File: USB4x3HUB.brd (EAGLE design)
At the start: 90 x 90 mm, 114 parts, among them IC1 TUSB2036, IC10 SN74LVC1G139DCUR, IC2 FSUSB74MPX, IC6 3.3V, IC7 5V, IC8 5V, IC9 5V, Q1 OSC4_6.0M, SW1 RD, SW2 BL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

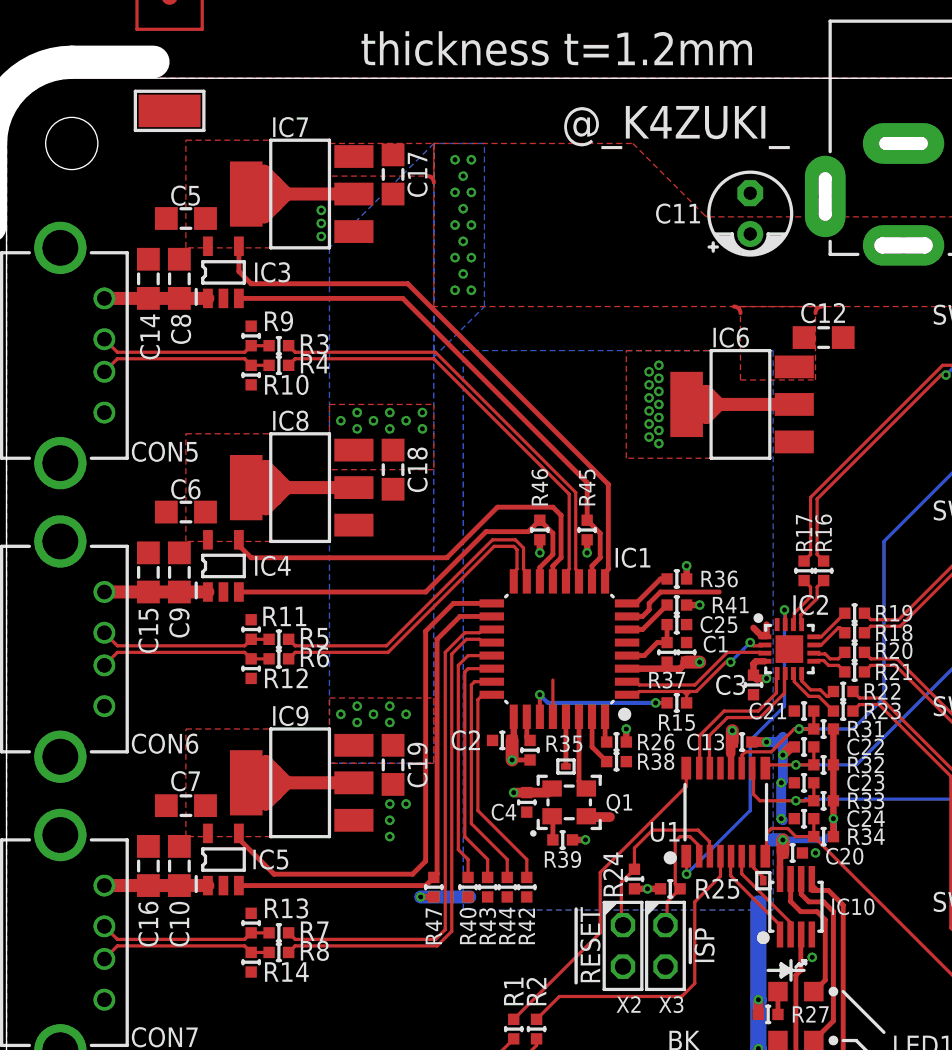
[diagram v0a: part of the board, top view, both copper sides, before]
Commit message: replace IC6-9 *CAUTION: airwires remain*
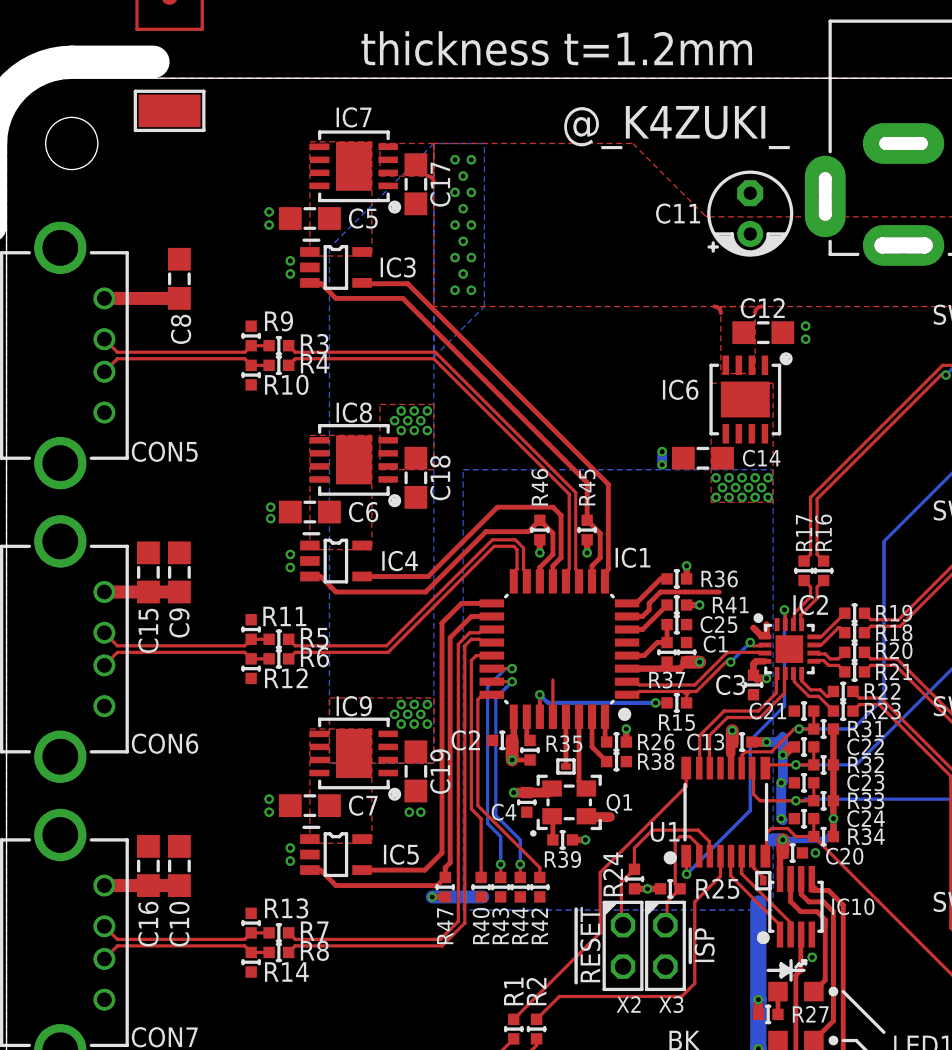
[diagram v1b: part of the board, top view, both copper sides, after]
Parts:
- IC6, IC7, IC8, IC9: device mylib:IC_SOT223 -> mylib:DFN80P410X410_8N
- moved C14 35.7 mm to (52.7, 56.7), turned to 180 degrees
- moved C5 7.60 mm to (28.6, 71.4)
- moved C6 7.60 mm to (28.6, 53.4)
- moved C7 7.60 mm to (28.6, 35.4)
- moved IC3 6.91 mm to (30.2, 68.4), turned to 270 degrees
- moved IC4 6.91 mm to (30.2, 50.4), turned to 270 degrees
- moved IC5 6.91 mm to (30.2, 32.4), turned to 270 degrees
- moved IC9 3.76 mm to (31.3, 38.6)
- moved C12 3.71 mm to (56.4, 64.4)
- moved IC8 3.71 mm to (31.3, 56.6)
- moved IC7 3.71 mm to (31.3, 74.6)
- moved C17 1.52 mm to (35.1, 73.5)
- moved C18 1.49 mm to (35.1, 55.5)
- moved C19 1.46 mm to (35.1, 37.5)
- moved R40 0.80 mm to (39.1, 30.4)
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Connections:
- net 3.3V: now also C14.1, IC6.5, IC6.6, IC6.7, IC6.EP; no longer IC6.2, IC6.4
- net 5V1: now also IC7.5, IC7.6, IC7.7, IC7.EP; no longer IC7.2, IC7.4
- net 5V2: now also IC8.5, IC8.6, IC8.7, IC8.EP; no longer IC8.2, IC8.4
- net 5V3: now also IC9.5, IC9.6, IC9.7, IC9.EP; no longer IC9.2, IC9.4
- net N$11: no longer C14.1
- net VIN: now also IC6.2, IC6.4, IC7.2, IC7.4, IC8.2, IC8.4, IC9.2, IC9.4
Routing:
- net 5V1: track 12.3 -> 0.00 mm
- net 5V3: track 11.8 -> 0.00 mm
- net 5V2: track 11.8 -> 0.00 mm
- net 3.3V: track 69.0 -> 58.6 mm, vias 32 -> 33
- net N$17: track 35.6 -> 26.2 mm
- net N$24: track 31.9 -> 23.0 mm
- net N$21: track 26.2 -> 18.4 mm
- net N$25: track 30.8 -> 26.8 mm
- net N$20: track 24.7 -> 20.7 mm
- net N$16: track 32.6 -> 28.7 mm
- net N$13: track 6.35 -> 4.60 mm
- net N$12: track 6.35 -> 4.60 mm
- net N$11: track 6.35 -> 4.60 mm
- net GND: track 21.1 -> 21.9 mm, vias 17 -> 28
- net N$64: track 15.5 -> 14.9 mm
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
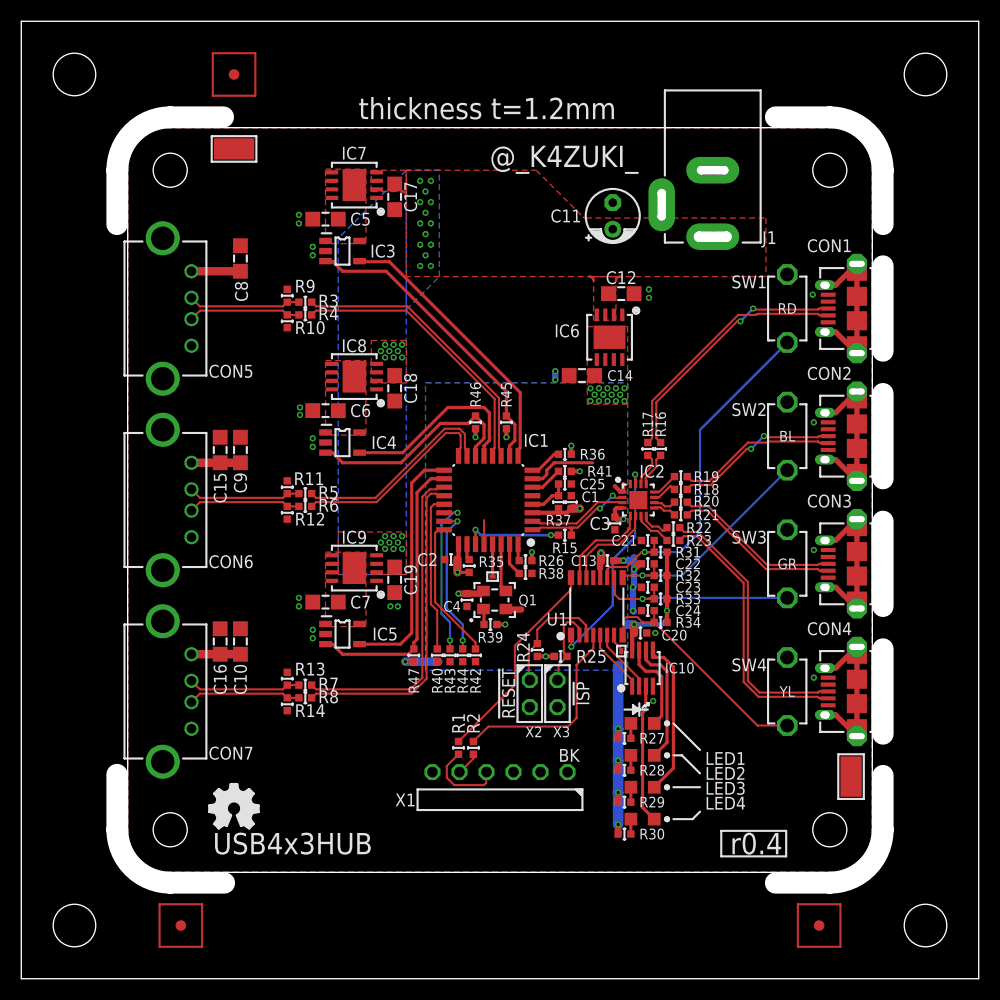
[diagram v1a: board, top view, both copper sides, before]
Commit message: C11: library update, C5-7 moved
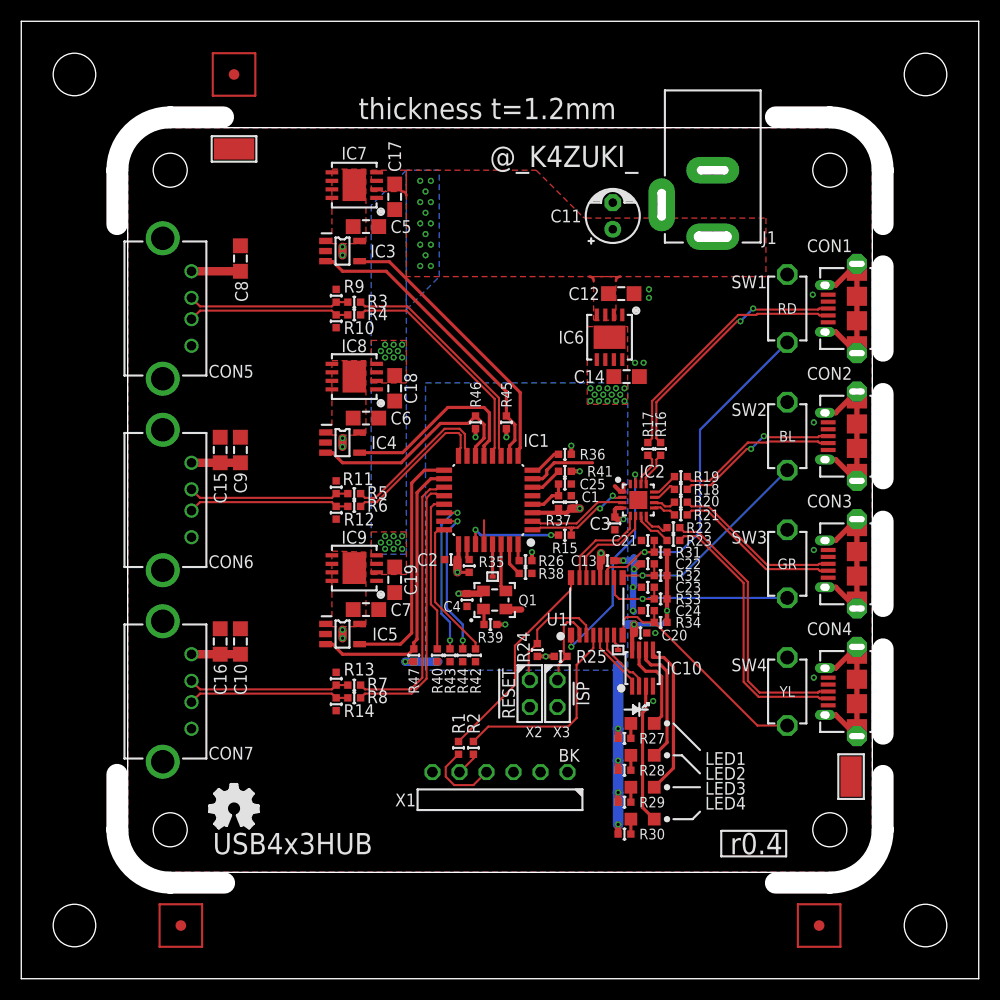
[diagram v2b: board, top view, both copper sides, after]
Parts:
- moved R10 4.60 mm to (29.6, 61.8)
- moved R11 4.60 mm to (29.6, 46.2)
- moved R12 4.60 mm to (29.6, 43.8)
- moved R13 4.60 mm to (29.6, 28.2)
- moved R14 4.60 mm to (29.6, 25.8)
- moved R3 4.60 mm to (31.3, 63.6)
- moved R4 4.60 mm to (31.3, 62.4)
- moved R5 4.60 mm to (31.3, 45.6)
- moved R6 4.60 mm to (31.3, 44.4)
- moved R7 4.60 mm to (31.3, 27.6)
- moved R8 4.60 mm to (31.3, 26.4)
- moved R9 4.60 mm to (29.6, 64.2)
- moved C14 4.20 mm to (56.9, 56.6), turned to 0 degrees
- moved C5 3.86 mm to (32.4, 70.7), turned to 0 degrees
- moved C6 3.86 mm to (32.4, 52.7), turned to 0 degrees
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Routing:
- net N$39: track 30.4 -> 25.8 mm
- net N$40: track 30.4 -> 25.8 mm
- net N$36: track 26.2 -> 21.6 mm
- net N$35: track 26.9 -> 22.3 mm
- net N$27: track 10.6 -> 15.2 mm
- net N$26: track 10.6 -> 15.2 mm
- net N$23: track 10.6 -> 15.2 mm
- net N$22: track 10.6 -> 15.2 mm
- net N$19: track 10.6 -> 15.2 mm
- net N$18: track 10.6 -> 15.2 mm
- net N$38: track 19.0 -> 14.4 mm
- net N$37: track 19.6 -> 15.0 mm
- net GND: track 21.9 -> 23.5 mm, vias 28 -> 20
- net ->TX: track 7.77 -> 7.27 mm

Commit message: C8-11 replaced by OS-CON 16V/100uF; PCB width shrinked 10mm(and necessary moves)
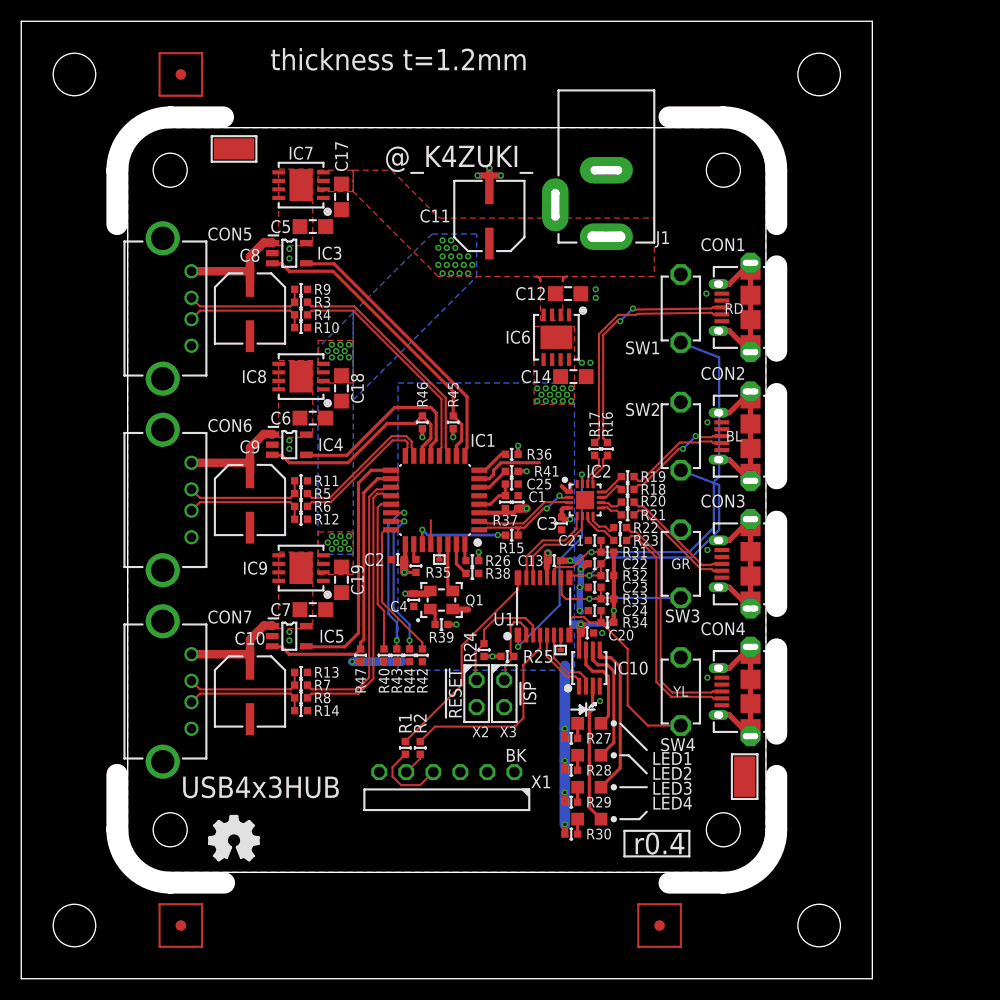
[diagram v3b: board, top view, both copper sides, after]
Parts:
- removed C15, C16: (no value), mylib:CR_2125
- removed PCB1: PCB_DP_SQUARE-7X7, dp_pcb:DP7070_V1
- C10, C8, C9: value (none) -> C_DENKAI_100U_2.5P6.3_C6; device mylib:CR_2125 -> mylib:C_2.5PHI6.3_C6
- C11: value C_DENKAI_100U_2.5P5 -> C_DENKAI_100U_2.5P6.3_C6; device mylib:C_2.5PHI5 -> mylib:C_2.5PHI6.3_C6
- moved TP101 15.0 mm to (60.0, 5.00)
- moved C11 11.6 mm to (44.0, 71.7), turned to 0 degrees
- moved CON1 10.0 mm to (70.0, 63.1)
- moved CON2 10.0 mm to (70.0, 51.0)
- moved CON3 10.0 mm to (70.0, 39.0)
- moved CON4 10.0 mm to (70.0, 27.0)
- moved J1 10.0 mm to (55.0, 83.5)
- moved SW1 10.0 mm to (62.0, 63.0)
- moved SW2 10.0 mm to (62.0, 51.0)
- moved SW3 10.0 mm to (62.0, 39.0)
- moved SW4 10.0 mm to (62.0, 27.0)
- moved TP1 10.0 mm to (68.0, 19.0)
- moved ICON2 9.10 mm to (60.0, 12.7)
- moved TP4 5.40 mm to (50.7, 30.9)
- moved TP3 5.25 mm to (39.3, 39.4)
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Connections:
- net GND: now also C10.-, C8.-, C9.-; no longer C10.2, C15.2, C16.2, C8.2, C9.2
- net N$11: now also C8.+; no longer C8.1
- net N$12: now also C9.+; no longer C15.1, C9.1
- net N$13: now also C10.+; no longer C10.1, C16.1
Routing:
- net N$11: track 4.60 -> 10.5 mm
- net N$13: track 4.60 -> 10.5 mm
- net N$12: track 4.60 -> 10.5 mm
- net SW1: track 34.2 -> 39.5 mm
- net SW3: track 20.2 -> 15.2 mm
- net N$9: track 15.8 -> 10.8 mm
- net N$7: track 15.7 -> 10.7 mm
- net N$6: track 15.0 -> 10.0 mm
- net N$5: track 15.4 -> 10.4 mm
- net SW2: track 21.9 -> 26.2 mm
- net N$23: track 15.2 -> 11.4 mm
- net N$22: track 15.2 -> 11.4 mm
- net N$19: track 15.2 -> 11.4 mm
- net N$18: track 15.2 -> 11.4 mm
- net N$27: track 15.2 -> 11.4 mm
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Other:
- board size 90 x 90 mm -> 80 x 90 mm

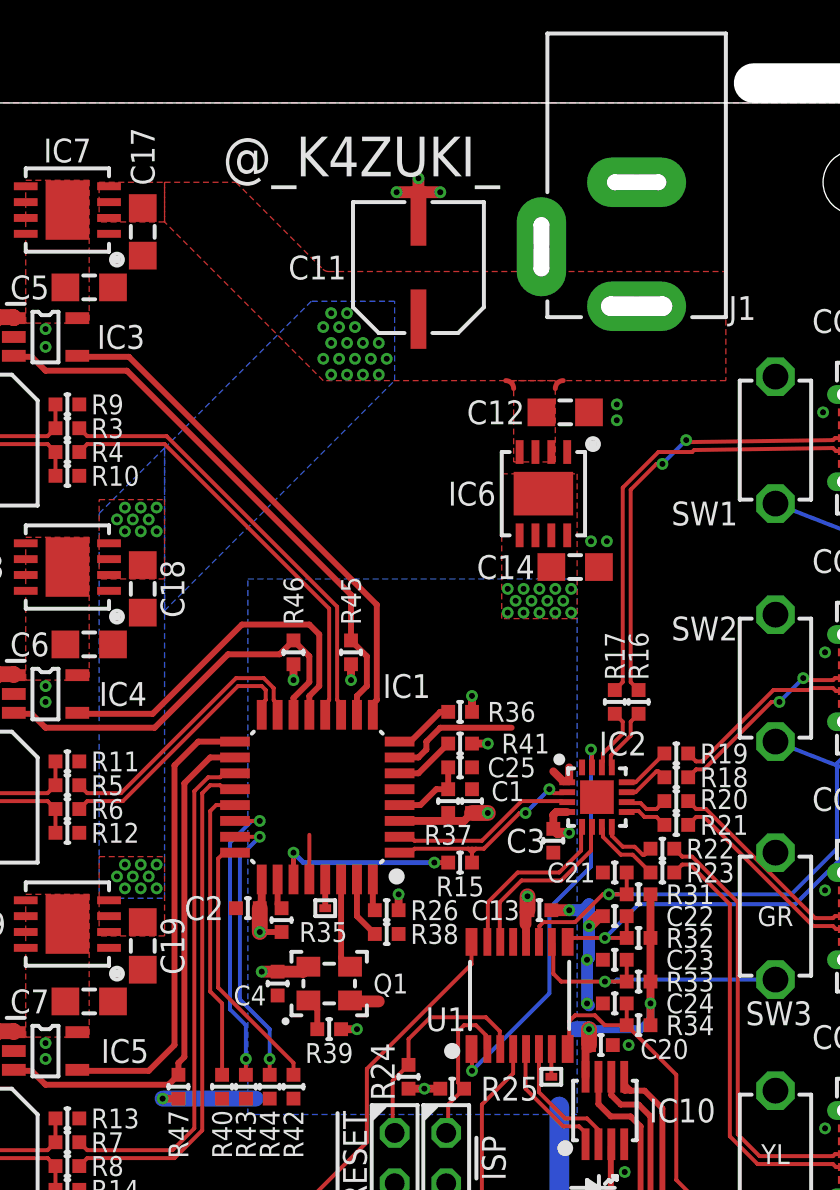
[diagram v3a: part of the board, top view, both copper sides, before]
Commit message: Capacitors renumbered
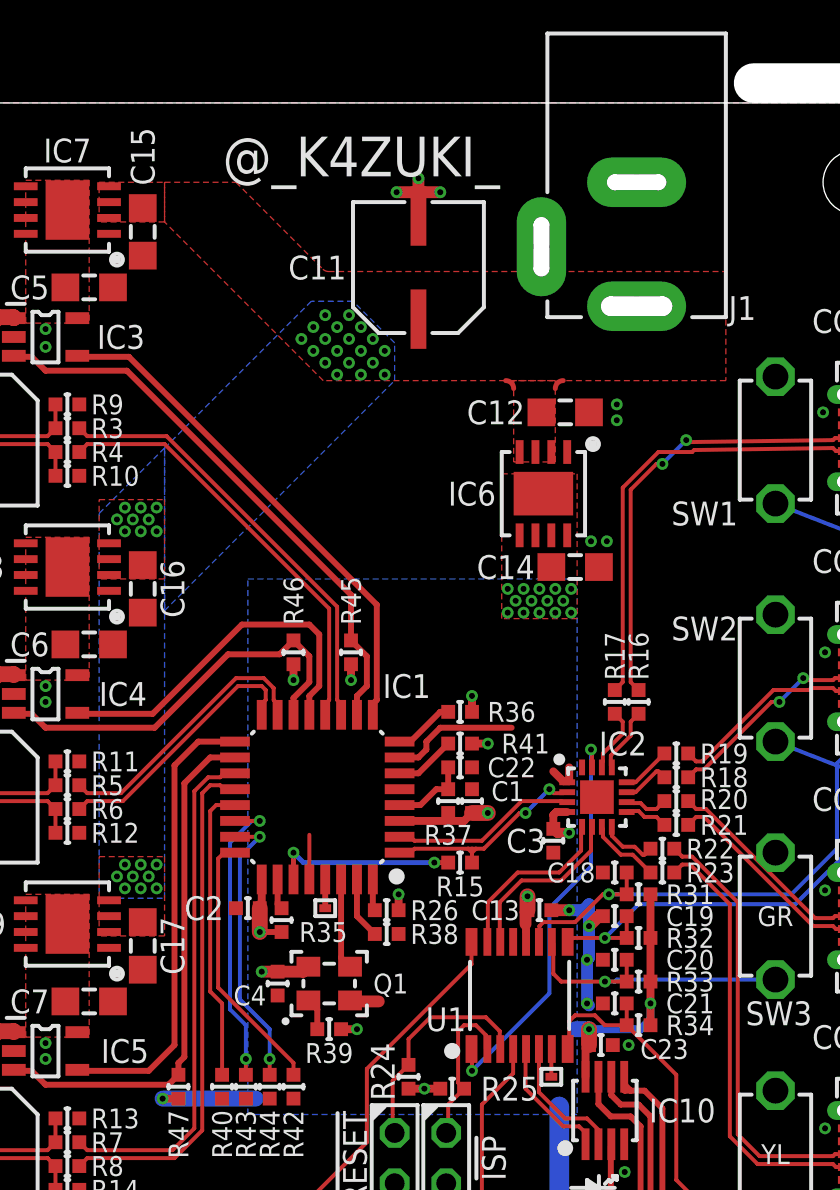
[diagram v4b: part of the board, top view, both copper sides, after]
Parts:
- removed C24: (no value), mylib:C0402
- removed C25: 1u/1005, mylib:C0402
- added C15, C16: (no value), mylib:CR_2125
- C18, C19: device mylib:CR_2125 -> mylib:C0402
- C22: value (none) -> 1u/1005
- moved C17 36.0 mm to (30.1, 37.5)
- moved C18 27.8 mm to (53.9, 41.2), turned to 180 degrees
- moved C19 23.8 mm to (53.9, 39.0), turned to 180 degrees
- moved C22 10.8 mm to (46.1, 46.5), turned to 0 degrees
- moved C21 6.60 mm to (53.9, 34.6)
- moved C20 4.36 mm to (53.9, 36.8), turned to 180 degrees
- moved C23 4.36 mm to (53.2, 32.5), turned to 0 degrees
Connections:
- net 3.3V: now also C23.1; no longer C20.1
- net GND: now also C15.2, C16.2; no longer C24.2, C25.2
- net N$62: now also C22.1; no longer C25.1
- net SW1: now also C18.1; no longer C21.1
- net SW2: now also C19.1; no longer C22.1
- net SW3: now also C20.1; no longer C23.1
- net SW4: now also C21.1; no longer C24.1
- net VIN: now also C15.1, C16.1; no longer C18.1, C19.1
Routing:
- net VIN: vias 36 -> 37
